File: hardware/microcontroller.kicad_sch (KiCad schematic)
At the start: 12 parts, among them SW1 SW_DPST, U1 ATSAMD21G18A-M, Y1 Crystal

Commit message: Net changes, sense changes
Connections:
- net MOSI: now reaches U1.19 (PB10)
- net SCK: now reaches U1.20 (PB11)
- net MISO: now reaches U1.21 (PA12)
- net SWCLK: now reaches U1.45 (PA30)
- net SWDIO: now reaches U1.46 (PA31)
- no-connect marks 27 -> 22
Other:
- moved on the sheet: R2, R3
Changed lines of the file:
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@@
   (no_connect (at 157.48 116.84))
   (no_connect (at 157.48 119.38))
-  (no_connect (at 157.48 88.9))
-  (no_connect (at 157.48 86.36))
   (no_connect (at 121.92 83.82))
   (no_connect (at 121.92 86.36))
   (no_connect (at 121.92 88.9))
-  (no_connect (at 121.92 91.44))
   (no_connect (at 121.92 93.98))
   (no_connect (at 157.48 66.04))
@@
   (no_connect (at 121.92 114.3))
   (no_connect (at 121.92 104.14))
-  (no_connect (at 121.92 139.7))
-  (no_connect (at 121.92 137.16))
   (no_connect (at 121.92 132.08))
   (no_connect (at 121.92 129.54))
@@
     (stroke (width 0) (type default) (color 0 0 0 0))
   )
+  (wire (pts (xy 165.1 81.28) (xy 157.48 81.28))
+    (stroke (width 0) (type default) (color 0 0 0 0))
+  )
   (wire (pts (xy 105.41 52.07) (xy 107.95 52.07))
     (stroke (width 0) (type default) (color 0 0 0 0))
@@
     (stroke (width 0) (type default) (color 0 0 0 0))
   )
+  (wire (pts (xy 165.1 83.82) (xy 157.48 83.82))
+    (stroke (width 0) (type default) (color 0 0 0 0))
+  )
   (wire (pts (xy 142.24 53.34) (xy 147.32 53.34))
     (stroke (width 0) (type default) (color 0 0 0 0))
@@
   )
   (wire (pts (xy 121.92 63.5) (xy 116.84 63.5))
+    (stroke (width 0) (type default) (color 0 0 0 0))
+  )
+  (wire (pts (xy 175.26 83.82) (xy 172.72 83.82))
+    (stroke (width 0) (type default) (color 0 0 0 0))
+  )
+  (wire (pts (xy 175.26 81.28) (xy 172.72 81.28))
     (stroke (width 0) (type default) (color 0 0 0 0))
   )
@@
     )
   )
+  (global_label "SWDIO" (shape output) (at 121.92 139.7 180) (fields_autoplaced)
+    (effects (font (size 1.27 1.27)) (justify right))
+    (property "Intersheet References" "${INTERSHEET_REFS}" (id 0) (at 113.6407 139.6206 0)
+      (effects (font (size 1.27 1.27)) (justify right) hide)
+    )
+  )
+  (global_label "SWCLK" (shape output) (at 121.92 137.16 180) (fields_autoplaced)
+    (effects (font (size 1.27 1.27)) (justify right))
+    (property "Intersheet References" "${INTERSHEET_REFS}" (id 0) (at 113.2779 137.0806 0)
+      (effects (font (size 1.27 1.27)) (justify right) hide)
+    )
+  )
   (global_label "UL" (shape output) (at 121.92 99.06 180) (fields_autoplaced)
     (effects (font (size 1.27 1.27)) (justify right))
@@
     )
   )
+  (global_label "MISO" (shape input) (at 121.92 91.44 180) (fields_autoplaced)
+    (effects (font (size 1.27 1.27)) (justify right))
+    (property "Intersheet References" "${INTERSHEET_REFS}" (id 0) (at 114.9107 91.3606 0)
+      (effects (font (size 1.27 1.27)) (justify right) hide)
+    )
+  )
   (global_label "ISNS_C" (shape input) (at 114.3 71.12 180) (fields_autoplaced)
     (effects (font (size 1.27 1.27)) (justify right))
@@
     )
   )
-  (global_label "ISNS_A" (shape input) (at 165.1 81.28 0) (fields_autoplaced)
+  (global_label "ISNS_A" (shape input) (at 175.26 81.28 0) (fields_autoplaced)
     (effects (font (size 1.27 1.27)) (justify left))
-    (property "Intersheet References" "${INTERSHEET_REFS}" (id 0) (at 173.9236 81.3594 0)
+    (property "Intersheet References" "${INTERSHEET_REFS}" (id 0) (at 184.0836 81.3594 0)
       (effects (font (size 1.27 1.27)) (justify left) hide)
     )
@@
     )
   )
-  (global_label "ISNS_B" (shape input) (at 165.1 83.82 0) (fields_autoplaced)
+  (global_label "SCK" (shape output) (at 157.48 88.9 0) (fields_autoplaced)
     (effects (font (size 1.27 1.27)) (justify left))
-    (property "Intersheet References" "${INTERSHEET_REFS}" (id 0) (at 174.105 83.8994 0)
+    (property "Intersheet References" "${INTERSHEET_REFS}" (id 0) (at 163.6426 88.8206 0)
+      (effects (font (size 1.27 1.27)) (justify left) hide)
+    )
+  )
+  (global_label "MOSI" (shape output) (at 157.48 86.36 0) (fields_autoplaced)
+    (effects (font (size 1.27 1.27)) (justify left))
+    (property "Intersheet References" "${INTERSHEET_REFS}" (id 0) (at 164.4893 86.2806 0)
+      (effects (font (size 1.27 1.27)) (justify left) hide)
+    )
+  )
+  (global_label "ISNS_B" (shape input) (at 175.26 83.82 0) (fields_autoplaced)
+    (effects (font (size 1.27 1.27)) (justify left))
+    (property "Intersheet References" "${INTERSHEET_REFS}" (id 0) (at 184.265 83.8994 0)
       (effects (font (size 1.27 1.27)) (justify left) hide)
     )
@@
     (pin "2")
   )
-  (symbol (lib_id "Device:R_US") (at 161.29 83.82 90) (unit 1)
+  (symbol (lib_id "Device:R_US") (at 168.91 83.82 90) (unit 1)
     (in_bom yes) (on_board yes)
-    (property "Reference" "R3" (id 0) (at 161.29 88.9 90))
-    (property "Value" "5k1" (id 1) (at 161.29 86.36 90))
-    (property "Footprint" "Resistor_SMD:R_0805_2012Metric" (id 2) (at 161.544 82.804 90)
-      (effects (font (size 1.27 1.27)) hide)
-    )
-    (property "Datasheet" "~" (id 3) (at 161.29 83.82 0)
-      (effects (font (size 1.27 1.27)) hide)
-    )
-    (property "Mouser" "https://www.mouser.com/ProductDetail/Panasonic/ERJ-6ENF5101V?qs=sGAEpiMZZMvdGkrng054t8AJgcdMkx7xVxAUQLZTFHA%3D" (id 4) (at 161.29 83.82 90)
+    (property "Reference" "R3" (id 0) (at 168.91 88.9 90))
+    (property "Value" "5k1" (id 1) (at 168.91 86.36 90))
+    (property "Footprint" "Resistor_SMD:R_0805_2012Metric" (id 2) (at 169.164 82.804 90)
+      (effects (font (size 1.27 1.27)) hide)
+    )
+    (property "Datasheet" "~" (id 3) (at 168.91 83.82 0)
+      (effects (font (size 1.27 1.27)) hide)
+    )
+    (property "Mouser" "https://www.mouser.com/ProductDetail/Panasonic/ERJ-6ENF5101V?qs=sGAEpiMZZMvdGkrng054t8AJgcdMkx7xVxAUQLZTFHA%3D" (id 4) (at 168.91 83.82 90)
       (effects (font (size 1.27 1.27)) hide)
     )
@@
     (pin "2")
   )
-  (symbol (lib_id "Device:R_US") (at 161.29 81.28 90) (unit 1)
-    (in_bom yes) (on_board yes) (fields_autoplaced)
-    (property "Reference" "R2" (id 0) (at 161.29 74.93 90))
-    (property "Value" "5k1" (id 1) (at 161.29 77.47 90))
-    (property "Footprint" "Resistor_SMD:R_0805_2012Metric" (id 2) (at 161.544 80.264 90)
-      (effects (font (size 1.27 1.27)) hide)
-    )
-    (property "Datasheet" "~" (id 3) (at 161.29 81.28 0)
-      (effects (font (size 1.27 1.27)) hide)
-    )
-    (property "Mouser" "https://www.mouser.com/ProductDetail/Panasonic/ERJ-6ENF5101V?qs=sGAEpiMZZMvdGkrng054t8AJgcdMkx7xVxAUQLZTFHA%3D" (id 4) (at 161.29 81.28 90)
-      (effects (font (size 1.27 1.27)) hide)
-    )
+  (symbol (lib_id "Device:R_US") (at 168.91 81.28 90) (unit 1)
+    (in_bom yes) (on_board yes)
+    (property "Reference" "R2" (id 0) (at 168.91 76.2 90))
+    (property "Value" "5k1" (id 1) (at 168.91 78.74 90))
+    (property "Footprint" "Resistor_SMD:R_0805_2012Metric" (id 2) (at 169.164 80.264 90)
+      (effects (font (size 1.27 1.27)) hide)
+    )
+    (property "Datasheet" "~" (id 3) (at 168.91 81.28 0)
+      (effects (font (size 1.27 1.27)) hide)
+    )
+    (property "Mouser" "https://www.mouser.com/ProductDetail/Panasonic/ERJ-6ENF5101V?qs=sGAEpiMZZMvdGkrng054t8AJgcdMkx7xVxAUQLZTFHA%3D" (id 4) (at 168.91 81.28 90)
+      (effects (font (size 1.27 1.27)) hide)
+    )

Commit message: swd interface
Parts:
- added J?: Conn_ARM_JTAG_SWD_10, Connector_PinHeader_1.27mm:PinHeader_2x05_P1.27mm_Vertical_SMD, symbol Connector:Conn_ARM_JTAG_SWD_10
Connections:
- net +3V3: now also J?.1 (VTref)
- net GND: now also J?.3 (GND), J?.5 (GND)
- net SWCLK: now also J?.4 (SWDCLK/TCK)
- net SWDIO: now also J?.2 (SWDIO/TMS)
- no-connect marks 22 -> 26
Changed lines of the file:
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@@
   (junction (at 95.25 52.07) (diameter 0) (color 0 0 0 0)
   )
+  (no_connect (at 60.96 127))
   (no_connect (at 121.92 66.04))
   (no_connect (at 121.92 68.58))
@@
   (no_connect (at 121.92 132.08))
   (no_connect (at 121.92 129.54))
+  (no_connect (at 76.2 104.14))
+  (no_connect (at 76.2 114.3))
+  (no_connect (at 76.2 116.84))
   (wire (pts (xy 132.08 31.75) (xy 143.51 31.75))
     (stroke (width 0) (type default) (color 0 0 0 0))
@@
     (stroke (width 0) (type default) (color 0 0 0 0))
   )
+  (wire (pts (xy 114.3 139.7) (xy 121.92 139.7))
+    (stroke (width 0) (type default) (color 0 0 0 0))
+  )
   (wire (pts (xy 175.26 83.82) (xy 172.72 83.82))
     (stroke (width 0) (type default) (color 0 0 0 0))
   )
+  (wire (pts (xy 114.3 137.16) (xy 121.92 137.16))
+    (stroke (width 0) (type default) (color 0 0 0 0))
+  )
+  (wire (pts (xy 76.2 111.76) (xy 85.09 111.76))
+    (stroke (width 0) (type default) (color 0 0 0 0))
+  )
   (wire (pts (xy 175.26 81.28) (xy 172.72 81.28))
     (stroke (width 0) (type default) (color 0 0 0 0))
@@
     (stroke (width 0) (type default) (color 0 0 0 0))
   )
+  (wire (pts (xy 76.2 109.22) (xy 85.09 109.22))
+    (stroke (width 0) (type default) (color 0 0 0 0))
+  )
   (wire (pts (xy 116.84 63.5) (xy 116.84 52.07))
     (stroke (width 0) (type default) (color 0 0 0 0))
@@
     (effects (font (size 1.27 1.27)) (justify left bottom))
   )
+  (label "SWDIO" (at 114.3 139.7 0)
+    (effects (font (size 1.27 1.27)) (justify left bottom))
+  )
+  (label "SWCLK" (at 85.09 109.22 180)
+    (effects (font (size 1.27 1.27)) (justify right bottom))
+  )
+  (label "SWDIO" (at 85.09 111.76 180)
+    (effects (font (size 1.27 1.27)) (justify right bottom))
+  )
   (label "D-" (at 111.76 121.92 0)
     (effects (font (size 1.27 1.27)) (justify left bottom))
@@
     (effects (font (size 1.27 1.27)) (justify left bottom))
   )
+  (label "SWCLK" (at 114.3 137.16 0)
+    (effects (font (size 1.27 1.27)) (justify left bottom))
+  )
   (global_label "VL" (shape output) (at 121.92 106.68 180) (fields_autoplaced)
     (effects (font (size 1.27 1.27)) (justify right))
@@
     (effects (font (size 1.27 1.27)) (justify right))
     (property "Intersheet References" "${INTERSHEET_REFS}" (id 0) (at 117.0274 109.1406 0)
-      (effects (font (size 1.27 1.27)) (justify right) hide)
-    )
-  )
-  (global_label "SWDIO" (shape output) (at 121.92 139.7 180) (fields_autoplaced)
-    (effects (font (size 1.27 1.27)) (justify right))
-    (property "Intersheet References" "${INTERSHEET_REFS}" (id 0) (at 113.6407 139.6206 0)
-      (effects (font (size 1.27 1.27)) (justify right) hide)
-    )
-  )
-  (global_label "SWCLK" (shape output) (at 121.92 137.16 180) (fields_autoplaced)
-    (effects (font (size 1.27 1.27)) (justify right))
-    (property "Intersheet References" "${INTERSHEET_REFS}" (id 0) (at 113.2779 137.0806 0)
       (effects (font (size 1.27 1.27)) (justify right) hide)
     )
@@
     (pin "2")
   )
+  (symbol (lib_id "Connector:Conn_ARM_JTAG_SWD_10") (at 63.5 111.76 0) (unit 1)
+    (in_bom yes) (on_board yes) (fields_autoplaced)
+    (property "Reference" "J?" (id 0) (at 52.07 110.4899 0)
+      (effects (font (size 1.27 1.27)) (justify right))
+    )
+    (property "Value" "Conn_ARM_JTAG_SWD_10" (id 1) (at 52.07 113.0299 0)
+      (effects (font (size 1.27 1.27)) (justify right))
+    )
+    (property "Footprint" "Connector_PinHeader_1.27mm:PinHeader_2x05_P1.27mm_Vertical_SMD" (id 2) (at 63.5 111.76 0)
+      (effects (font (size 1.27 1.27)) hide)
+    )
+    (property "Datasheet" "http://infocenter.arm.com/help/topic/com.arm.doc.ddi0314h/DDI0314H_coresight_components_trm.pdf" (id 3) (at 54.61 143.51 90)
+      (effects (font (size 1.27 1.27)) hide)
+    )
+    (pin "1")
+    (pin "10")
+    (pin "2")
+    (pin "3")
+    (pin "4")
+    (pin "5")
+    (pin "6")
+    (pin "7")
+    (pin "8")
+    (pin "9")
+  )
   (symbol (lib_id "power:GND") (at 107.95 59.69 0) (unit 1)
     (in_bom yes) (on_board yes) (fields_autoplaced)
@@
     (pin "2")
   )
+  (symbol (lib_id "power:GND") (at 63.5 127 0) (unit 1)
+    (in_bom yes) (on_board yes) (fields_autoplaced)
+    (property "Reference" "#PWR?" (id 0) (at 63.5 133.35 0)
+      (effects (font (size 1.27 1.27)) hide)
+    )
+    (property "Value" "GND" (id 1) (at 63.5 132.08 0))
+    (property "Footprint" "" (id 2) (at 63.5 127 0)
+      (effects (font (size 1.27 1.27)) hide)
+    )
+    (property "Datasheet" "" (id 3) (at 63.5 127 0)
+      (effects (font (size 1.27 1.27)) hide)
+    )
+    (pin "1")
+  )
   (symbol (lib_id "power:GND") (at 95.25 59.69 0) (unit 1)
     (in_bom yes) (on_board yes) (fields_autoplaced)
@@
     (pin "2")
   )
+  (symbol (lib_id "power:+3V3") (at 63.5 96.52 0) (unit 1)
+    (in_bom yes) (on_board yes) (fields_autoplaced)
+    (property "Reference" "#PWR?" (id 0) (at 63.5 100.33 0)
+      (effects (font (size 1.27 1.27)) hide)
+    )
+    (property "Value" "+3V3" (id 1) (at 63.5 91.44 0))
+    (property "Footprint" "" (id 2) (at 63.5 96.52 0)
+      (effects (font (size 1.27 1.27)) hide)
+    )
+    (property "Datasheet" "" (id 3) (at 63.5 96.52 0)
+      (effects (font (size 1.27 1.27)) hide)
+    )
+    (pin "1")
+  )
   (symbol (lib_id "power:+3V3") (at 111.76 139.7 0) (unit 1)

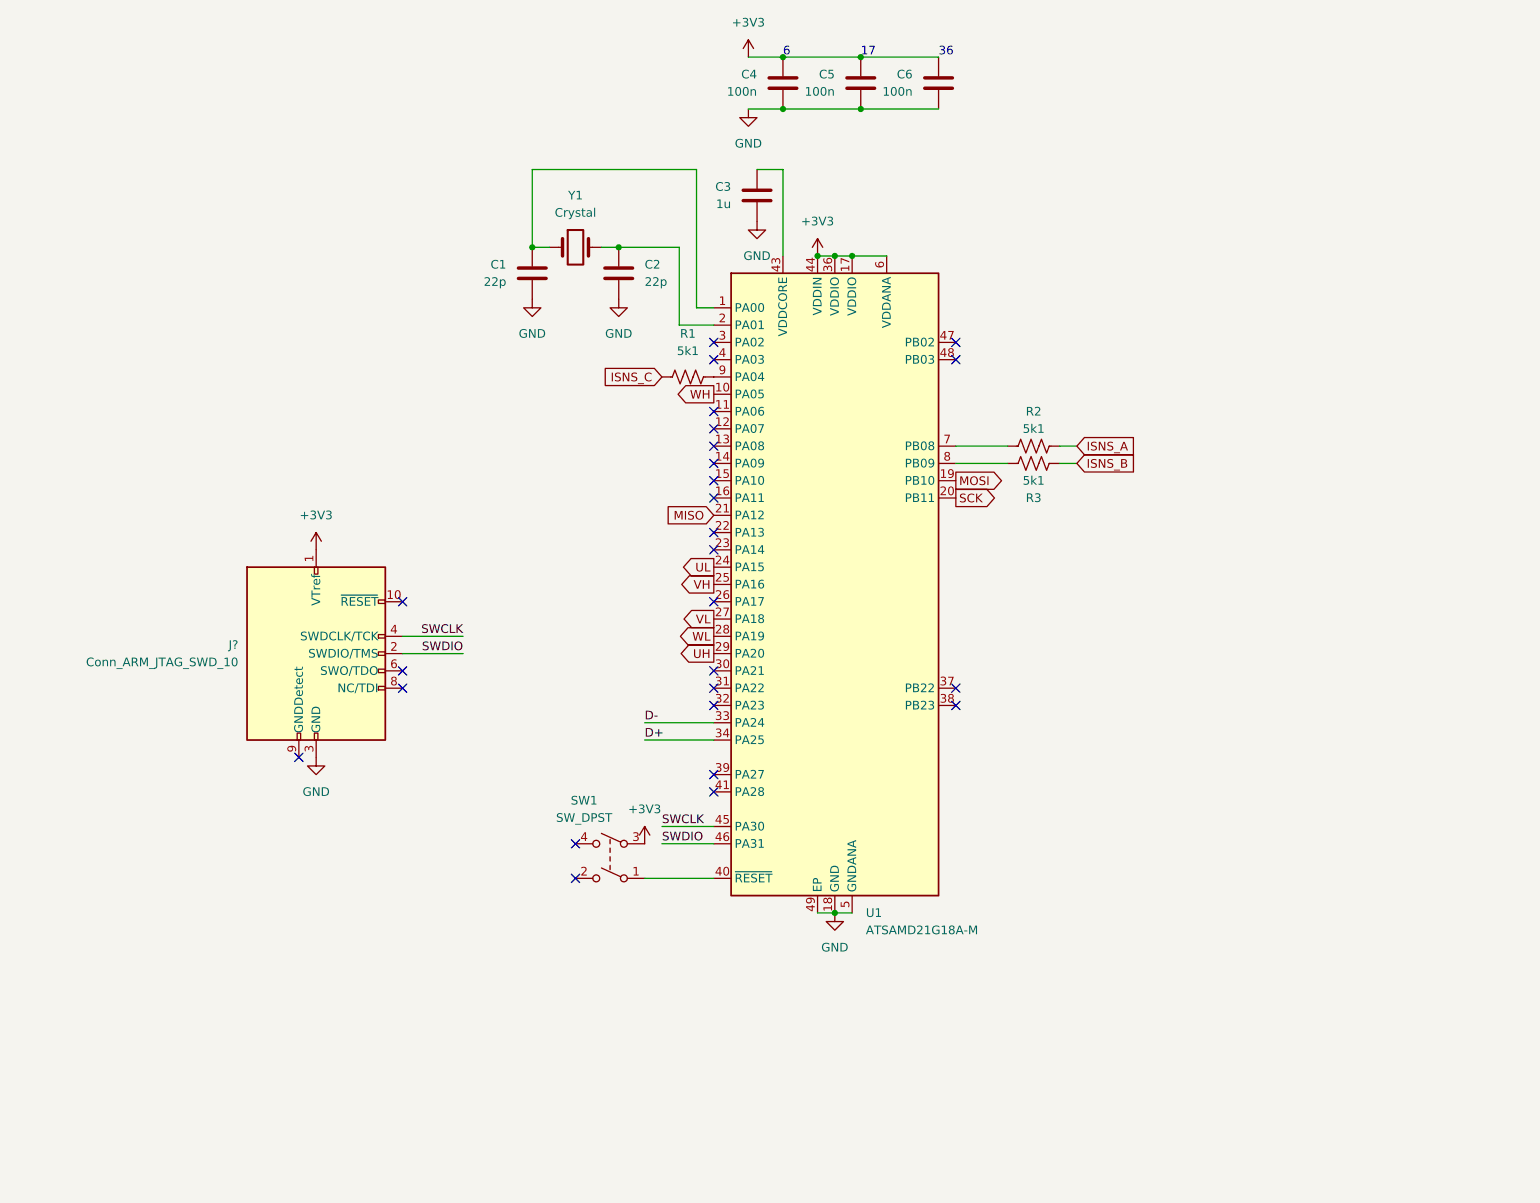
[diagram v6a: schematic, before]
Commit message: cleanup microcontroller sheet and increase verbosity
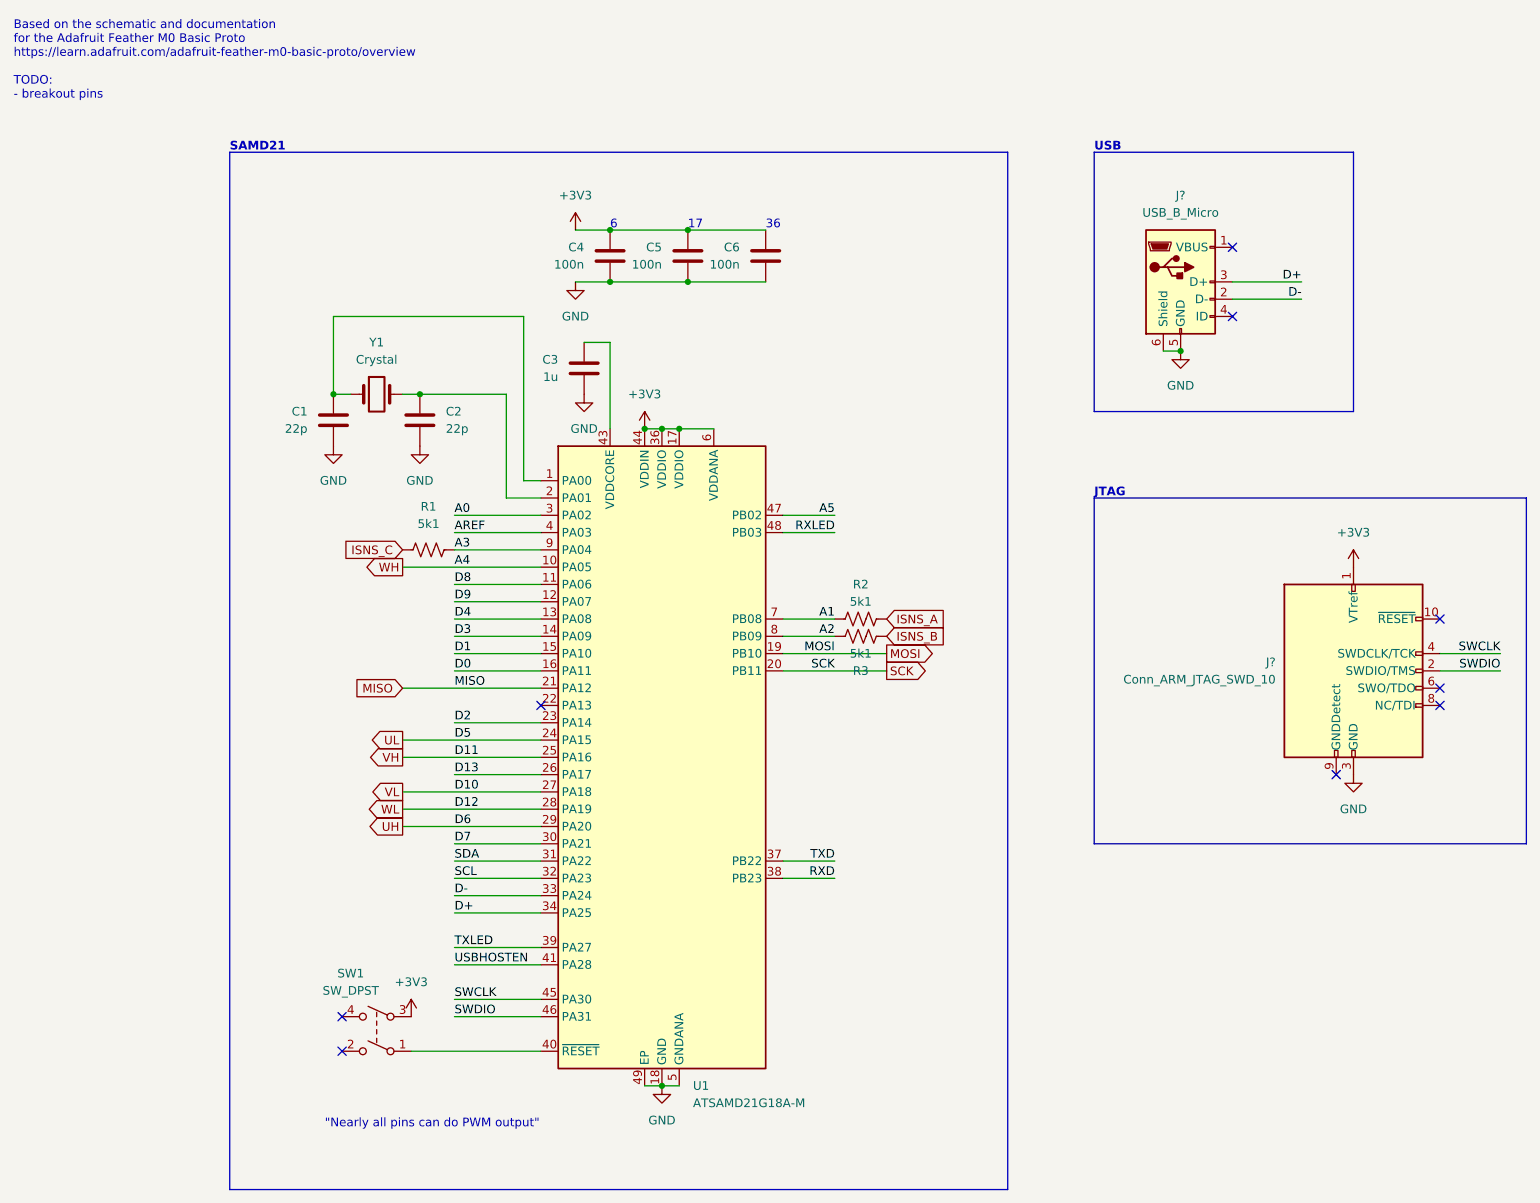
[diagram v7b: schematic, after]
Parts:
- added J?: USB_B_Micro, Connector_USB:USB_Micro-B_Molex_47346-0001, symbol Connector:USB_B_Micro
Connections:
- net D+: now also J?.3 (D+)
- net D-: now also J?.2 (D-)
- net GND: now also J?.5 (GND), J?.6 (Shield)
- net A2: now reaches R3.1, U1.8 (PB09)
- net A3: now reaches R1.2, U1.9 (PA04)
- net A1: now reaches R2.1, U1.7 (PB08)
- net D8: now reaches U1.11 (PA06)
- net D9: now reaches U1.12 (PA07)
- net D4: now reaches U1.13 (PA08)
- net D3: now reaches U1.14 (PA09)
- net D1: now reaches U1.15 (PA10)
- net D0: now reaches U1.16 (PA11)
- net D2: now reaches U1.23 (PA14)
- net D13: now reaches U1.26 (PA17)
- net A0: now reaches U1.3 (PA02)
- net D7: now reaches U1.30 (PA21)
- net SDA: now reaches U1.31 (PA22)
- net SCL: now reaches U1.32 (PA23)
- net TXD: now reaches U1.37 (PB22)
- net RXD: now reaches U1.38 (PB23)
- net TXLED: now reaches U1.39 (PA27)
- net AREF: now reaches U1.4 (PA03)
- net USBHOSTEN: now reaches U1.41 (PA28)
- net A5: now reaches U1.47 (PB02)
- net RXLED: now reaches U1.48 (PB03)
- no-connect marks 26 -> 9
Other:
- note added: ""Nearly all pins can do PWM output""
- note added: "Based on the schematic and documentation for the Adafruit Feather M0 Basic Proto https://learn.adafruit.com/adafruit-feather-m0-basic-proto/overview TODO: - breakout pins"
- note added: "JTAG"
- note added: "SAMD21"
- note added: "USB"
- moved on the sheet: C1, C2, C3, C4, C5, C6, J?, R1, R2, R3, SW1, U1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

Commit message: some layout
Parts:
- C1, C2: footprint Capacitor_SMD:C_0402_1005Metric_Pad0.74x0.62mm_HandSolder -> Capacitor_SMD:C_0805_2012Metric; Mouser https://www.mouser.com/ProductDetail/Murata-Electronics/GCM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 -> https://www.mouser.com/ProductDetail/Murata-Electronics/GQM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
- C3: footprint Capacitor_SMD:C_0402_1005Metric -> Capacitor_SMD:C_0805_2012Metric; Mouser https://www.mouser.com/ProductDetail/Murata-Electronics/GCM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 -> https://www.mouser.com/ProductDetail/Murata-Electronics/GRM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
- C4, C5, C6: footprint Capacitor_SMD:C_0402_1005Metric -> Capacitor_SMD:C_0805_2012Metric; Mouser https://www.mouser.com/ProductDetail/Murata-Electronics/GCM155R71E104KE02D?qs=sGAEpiMZZMvsSlwiRhF8qsL%2Fc0EXNue%2FoQ0bAUFzBJynJfbvKN%252BGCA%3D%3D -> https://www.mouser.com/ProductDetail/Murata-Electronics/GCM21BR72A104KA37L?qs=sGAEpiMZZMvsSlwiRhF8qh1EJ90GfnwbFI4pHbW65Ww%3D
- gave numbers to parts that had none: 2
